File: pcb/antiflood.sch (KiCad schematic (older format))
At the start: 92 parts, among them J1 Barrel_Jack, J10 Screw_Terminal_01x02, J11 Screw_Terminal_01x02, J12 Screw_Terminal_01x02, J13 Screw_Terminal_01x02, J2 01x03, J3 01x03, J4 Conn_02x05_Odd_Even, J5 Conn_02x04_Odd_Even, J6 Conn_02x05_Odd_Even, J7 Conn_02x03_Odd_Even, J8 Screw_Terminal_01x02, J9 Screw_Terminal_01x02, K1 P-5, K2 P-5, Q1 2N3904, Q2 2N3904, SW1 SW_Push, SW2 SW_Push, SW3 SW_Push, U1 LM1117-3.3, U2 ATMEGA328P-AU, U3 LM7805_TO220, U4 MC34063, U6 TP4056, Y1 16MHz

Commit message: Update.
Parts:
- added R? (x2): 10k, symbol R
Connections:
- wire segments 324 -> 326
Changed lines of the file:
@@
 	3800 3300 3800 2600
 Wire Wire Line
-	3800 2600 4700 2600
+	3800 2600 4800 2600
 Connection ~ 4700 2600
 Wire Wire Line
@@
 	3800 3850 3800 3950
 Wire Wire Line
-	3600 3950 4700 3950
+	3600 3950 4800 3950
 Connection ~ 4700 3950
 Wire Wire Line
@@
 Wire Wire Line
 	3600 2950 3900 2950
+$Comp
+L R R?
+U 1 1 5CB71E28
+P 4950 2600
+F 0 "R?" V 5030 2600 50  0000 C CNN
+F 1 "10k" V 4950 2600 50  0000 C CNN
+F 2 "" V 4880 2600 50  0001 C CNN
+F 3 "" H 4950 2600 50  0001 C CNN
+	1    4950 2600
+	0    -1   -1   0
+$EndComp
+$Comp
+L R R?
+U 1 1 5CB72139
+P 4950 3950
+F 0 "R?" V 5030 3950 50  0000 C CNN
+F 1 "10k" V 4950 3950 50  0000 C CNN
+F 2 "" V 4880 3950 50  0001 C CNN
+F 3 "" H 4950 3950 50  0001 C CNN
+	1    4950 3950
+	0    1    1    0
+$EndComp
+Wire Wire Line
+	5100 3950 5350 3950
+Wire Wire Line
+	5100 2600 5350 2600
+Text Label 5150 3950 0    60   ~ 0
+BSTE
+Text Label 5150 2600 0    60   ~ 0
+CHGE
 $EndSCHEMATC

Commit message: Update: remove linear regul
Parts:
- removed U3: LM7805_TO220, TO_SOT_Packages_THT:TO-220-3_Horizontal, symbol LM7805_TO220
- R?: value R -> 10k
- R?: value R -> 12k
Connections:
- wire segments 326 -> 427

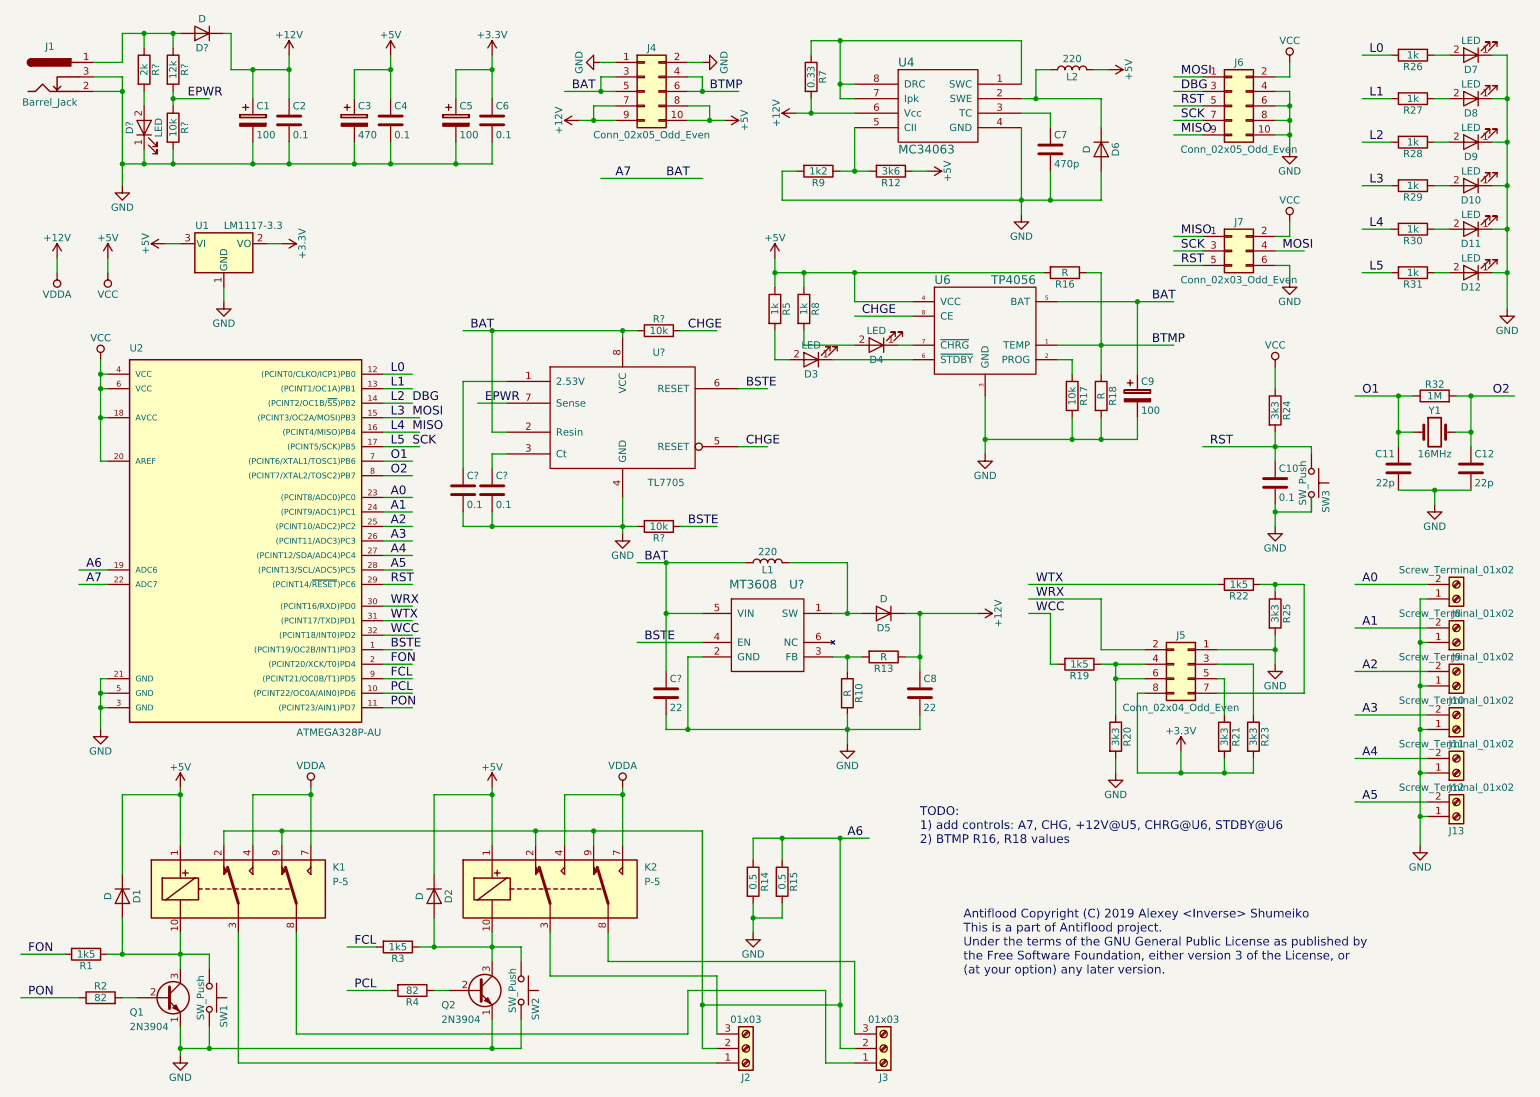
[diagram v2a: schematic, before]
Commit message: Update: pcb-bat connection
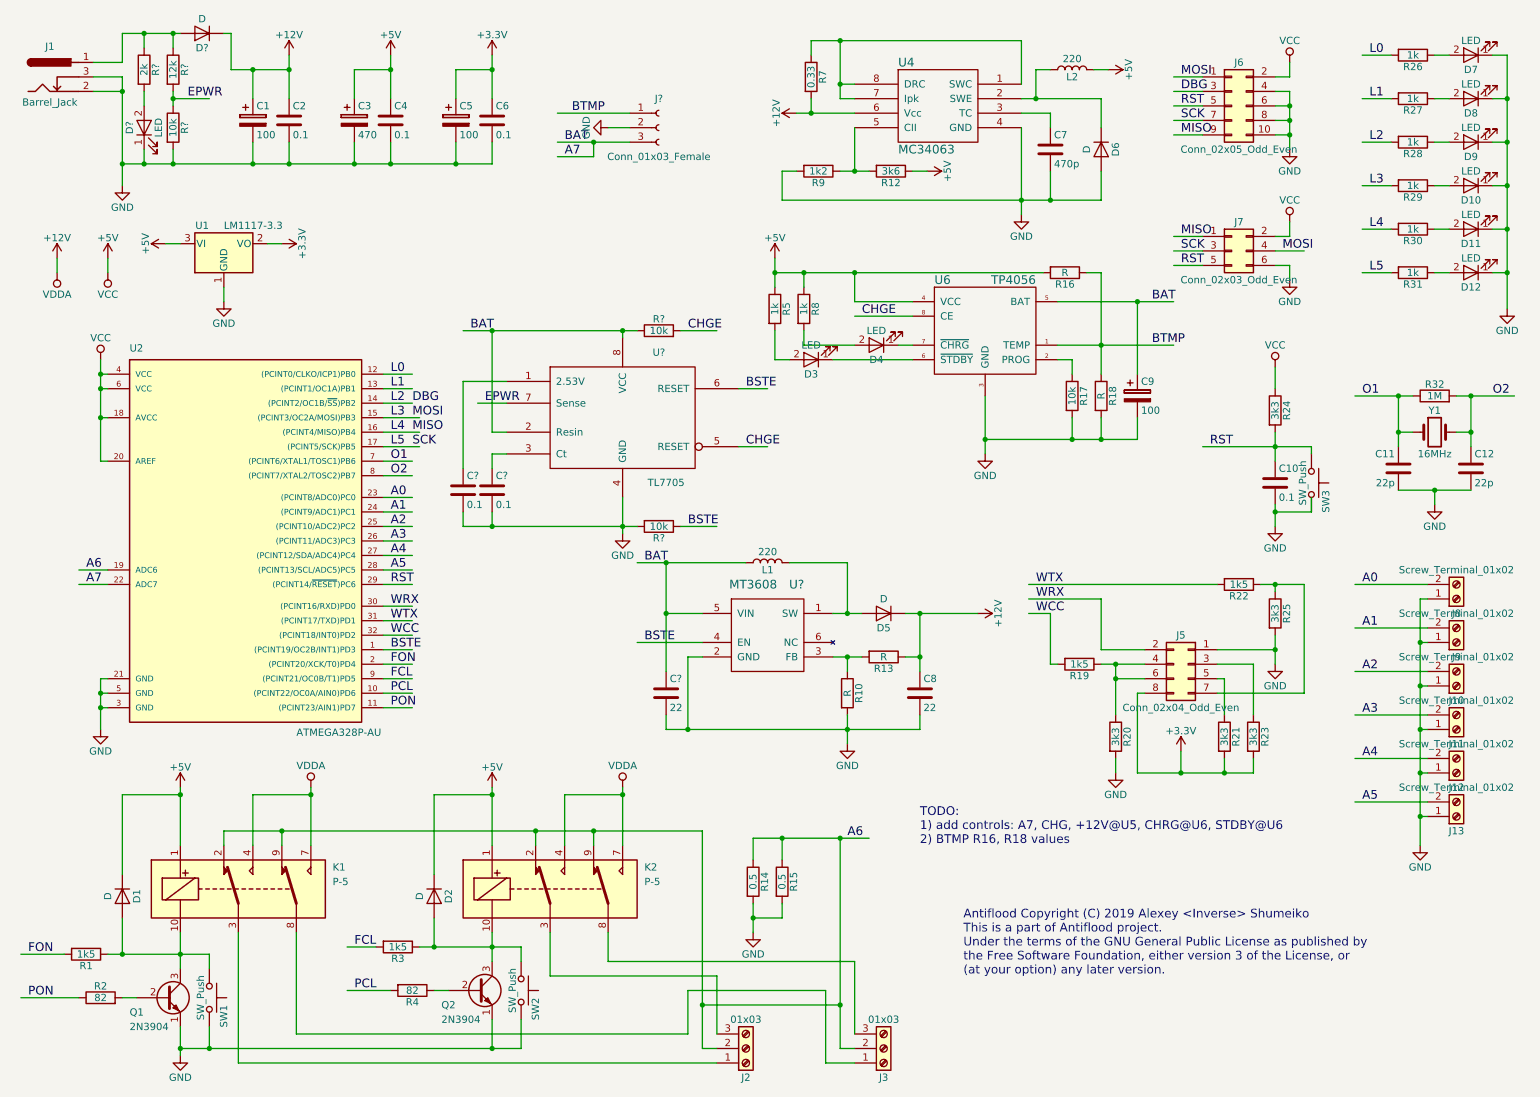
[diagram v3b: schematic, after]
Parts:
- removed J4: Conn_02x05_Odd_Even, Socket_Strips:Socket_Strip_Straight_2x05_Pitch2.54mm, symbol Conn_02x05_Odd_Even
- added J?: Conn_01x03_Female, symbol Conn_01x03_Female
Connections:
- wire segments 427 -> 313

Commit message: Update scheme.
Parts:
- removed D5: D, Diodes_SMD:D_SMA, symbol D
- removed D?: D, symbol D
- removed J?: Conn_01x03_Female, symbol Conn_01x03_Female
- added D?: ???, symbol D_Schottky_x2_KCom_AAK
- added J?: Conn_01x03_Male, symbol Conn_01x03_Male
- added R?: 1k, symbol R
- R10: value R -> 1k05
- R13: value R -> 20k
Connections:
- net labels added: EVSS
- wire segments 313 -> 315
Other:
- note removed: "TODO:\n1) add controls: A7, CHG, +12V@U5, CHRG@U6, STDBY@U6\n2) BTMP R16, R18 values"
- moved on the sheet: U1
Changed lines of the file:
@@
 L +12V #PWR06
 U 1 1 5B464A99
-P 800 2100
-F 0 "#PWR06" H 800 1950 50  0001 C CNN
-F 1 "+12V" H 800 2240 50  0000 C CNN
-F 2 "" H 800 2100 50  0001 C CNN
-F 3 "" H 800 2100 50  0001 C CNN
-	1    800  2100
-	1    0    0    -1
+P 4800 2100
+F 0 "#PWR06" H 4800 1950 50  0001 C CNN
+F 1 "+12V" H 4800 2240 50  0000 C CNN
+F 2 "" H 4800 2100 50  0001 C CNN
+F 3 "" H 4800 2100 50  0001 C CNN
+	1    4800 2100
+	0    -1   -1   0
 $EndComp
 $Comp
 L VDDA #PWR07
 U 1 1 5B464B17
-P 800 2200
-F 0 "#PWR07" H 800 2050 50  0001 C CNN
-F 1 "VDDA" H 800 2350 50  0000 C CNN
-F 2 "" H 800 2200 50  0001 C CNN
-F 3 "" H 800 2200 50  0001 C CNN
-	1    800  2200
-	-1   0    0    1
+P 4900 2100
+F 0 "#PWR07" H 4900 1950 50  0001 C CNN
+F 1 "VDDA" H 4900 2250 50  0000 C CNN
+F 2 "" H 4900 2100 50  0001 C CNN
+F 3 "" H 4900 2100 50  0001 C CNN
+	1    4900 2100
+	0    1    1    0
 $EndComp
 $Comp
@@
 L LM1117-3.3 U1
 U 1 1 5B469F43
-P 1950 2000
-F 0 "U1" H 1800 2125 50  0000 C CNN
-F 1 "LM1117-3.3" H 1950 2125 50  0000 L CNN
-F 2 "TO_SOT_Packages_SMD:SOT-223-3_TabPin2" H 1950 2000 50  0001 C CNN
-F 3 "" H 1950 2000 50  0001 C CNN
-	1    1950 2000
+P 4850 850
+F 0 "U1" H 4700 975 50  0000 C CNN
+F 1 "LM1117-3.3" H 4850 975 50  0000 L CNN
+F 2 "TO_SOT_Packages_SMD:SOT-223-3_TabPin2" H 4850 850 50  0001 C CNN
+F 3 "" H 4850 850 50  0001 C CNN
+	1    4850 850
 	1    0    0    -1
 $EndComp
@@
 L VCC #PWR09
 U 1 1 5B480980
-P 1150 2200
-F 0 "#PWR09" H 1150 2050 50  0001 C CNN
-F 1 "VCC" H 1150 2350 50  0000 C CNN
-F 2 "" H 1150 2200 50  0001 C CNN
-F 3 "" H 1150 2200 50  0001 C CNN
-	1    1150 2200
-	-1   0    0    1
+P 4900 1750
+F 0 "#PWR09" H 4900 1600 50  0001 C CNN
+F 1 "VCC" H 4900 1900 50  0000 C CNN
+F 2 "" H 4900 1750 50  0001 C CNN
+F 3 "" H 4900 1750 50  0001 C CNN
+	1    4900 1750
+	0    1    1    0
 $EndComp
 $Comp
 L +5V #PWR010
 U 1 1 5B480B0B
-P 1150 2100
-F 0 "#PWR010" H 1150 1950 50  0001 C CNN
-F 1 "+5V" H 1150 2240 50  0000 C CNN
-F 2 "" H 1150 2100 50  0001 C CNN
-F 3 "" H 1150 2100 50  0001 C CNN
-	1    1150 2100
-	1    0    0    -1
+P 4800 1750
+F 0 "#PWR010" H 4800 1600 50  0001 C CNN
+F 1 "+5V" H 4800 1890 50  0000 C CNN
+F 2 "" H 4800 1750 50  0001 C CNN
+F 3 "" H 4800 1750 50  0001 C CNN
+	1    4800 1750
+	0    -1   -1   0
 $EndComp
 $Comp
@@
 	1    0    0    -1
 $EndComp
-Text Notes 6750 6150 0    60   ~ 0
-TODO:\n1) add controls: A7, CHG, +12V@U5, CHRG@U6, STDBY@U6\n2) BTMP R16, R18 values
 $Comp
 L C C6
@@
 L GND #PWR036
 U 1 1 5C9B1BA9
-P 1950 2400
-F 0 "#PWR036" H 1950 2150 50  0001 C CNN
-F 1 "GND" H 1950 2250 50  0000 C CNN
-F 2 "" H 1950 2400 50  0001 C CNN
-F 3 "" H 1950 2400 50  0001 C CNN
-	1    1950 2400
+P 4850 1250
+F 0 "#PWR036" H 4850 1000 50  0001 C CNN
+F 1 "GND" H 4850 1100 50  0000 C CNN
+F 2 "" H 4850 1250 50  0001 C CNN
+F 3 "" H 4850 1250 50  0001 C CNN
+	1    4850 1250
 	1    0    0    -1
 $EndComp
@@
 P 6250 5100
 F 0 "R10" V 6330 5100 50  0000 C CNN
-F 1 "R" V 6250 5100 50  0000 C CNN
+F 1 "1k05" V 6250 5100 50  0000 C CNN
 F 2 "Resistors_SMD:R_0805" V 6180 5100 50  0001 C CNN
 F 3 "" H 6250 5100 50  0001 C CNN
@@
 P 6500 4850
 F 0 "R13" V 6580 4850 50  0000 C CNN
-F 1 "R" V 6500 4850 50  0000 C CNN
+F 1 "20k" V 6500 4850 50  0000 C CNN
 F 2 "Resistors_SMD:R_0805" V 6430 4850 50  0001 C CNN
 F 3 "" H 6500 4850 50  0001 C CNN
@@
 $EndComp
 $Comp
-L D D5
-U 1 1 5CAB0B56
-P 6500 4550
-F 0 "D5" H 6500 4650 50  0000 C CNN
-F 1 "D" H 6500 4450 50  0000 C CNN
-F 2 "Diodes_SMD:D_SMA" H 6500 4550 50  0001 C CNN
-F 3 "" H 6500 4550 50  0001 C CNN
-	1    6500 4550
-	-1   0    0    1
-$EndComp
-$Comp
 L GND #PWR046
 U 1 1 5CAB0B68
@@
 L +12V #PWR048
 U 1 1 5CAB3382
-P 7150 4550
-F 0 "#PWR048" H 7150 4400 50  0001 C CNN
-F 1 "+12V" H 7150 4690 50  0000 C CNN
-F 2 "" H 7150 4550 50  0001 C CNN
-F 3 "" H 7150 4550 50  0001 C CNN
-	1    7150 4550
-	0    1    1    0
+P 6650 4250
+F 0 "#PWR048" H 6650 4100 50  0001 C CNN
+F 1 "+12V" H 6650 4390 50  0000 C CNN
+F 2 "" H 6650 4250 50  0001 C CNN
+F 3 "" H 6650 4250 50  0001 C CNN
+	1    6650 4250
+	1    0    0    -1
 $EndComp
 $Comp
@@
 Text Label 4850 4200 0    60   ~ 0
 BAT
-$Comp
-L D D?
-U 1 1 5CB0165B
-P 1800 550
-F 0 "D?" H 1800 650 50  0000 C CNN
-F 1 "D" H 1800 450 50  0000 C CNN
-F 2 "" H 1800 550 50  0001 C CNN
-F 3 "" H 1800 550 50  0001 C CNN
-	1    1800 550
-	-1   0    0    1
-$EndComp
 $Comp
 L R R?
@@
 	9200 2150 9300 2150
 Wire Wire Line
-	1150 2100 1150 2200
+	4800 1750 4900 1750
 Wire Wire Line
 	3050 3600 3250 3600
@@
 	950  4350 1150 4350
 Wire Wire Line
-	800  2100 800  2200
+	4800 2100 4900 2100
 Connection ~ 1250 950
 Wire Wire Line
@@
 Wire Wire Line
 	2150 1000 2150 800
-Wire Wire Line
-	2000 800  2400 800
 Connection ~ 2400 800
 Wire Wire Line
@@
 Connection ~ 3800 800
 Wire Wire Line
-	1550 2000 1650 2000
-Wire Wire Line
-	2250 2000 2350 2000
-Wire Wire Line
-	1950 2300 1950 2400
+	4450 850  4550 850
+Wire Wire Line
+	5150 850  5250 850
+Wire Wire Line
+	4850 1150 4850 1250
 Wire Wire Line
 	5900 1100 6300 1100
@@
 Connection ~ 6250 4550
 Wire Wire Line
-	6650 4550 7150 4550
-Wire Wire Line
 	6250 4200 5850 4200
 Wire Wire Line
-	6750 4550 6750 4950
-Wire Wire Line
-	6750 4850 6650 4850
-Connection ~ 6750 4550
+	6750 4850 6750 4950
+Wire Wire Line
+	6650 4850 7050 4850
 Connection ~ 6750 4850
 Wire Wire Line
@@
 Wire Wire Line
 	1250 750  1250 550
-Connection ~ 2150 800
 Wire Wire Line
 	1600 550  1600 650
@@
 Connection ~ 1600 1000
 Wire Wire Line
-	1250 550  1650 550
+	1250 550  1850 550
 Wire Wire Line
 	1250 1450 3800 1450
-Wire Wire Line
-	1950 550  2000 550
-Wire Wire Line
-	2000 550  2000 800
 Wire Wire Line
 	1400 650  1400 550
@@
 L +3.3V #PWR032
 U 1 1 5C9B0B9F
-P 2350 2000
-F 0 "#PWR032" H 2350 1850 50  0001 C CNN
-F 1 "+3.3V" H 2350 2140 50  0000 C CNN
-F 2 "" H 2350 2000 50  0001 C CNN
-F 3 "" H 2350 2000 50  0001 C CNN
-	1    2350 2000
+P 5250 850
+F 0 "#PWR032" H 5250 700 50  0001 C CNN
+F 1 "+3.3V" H 5250 990 50  0000 C CNN
+F 2 "" H 5250 850 50  0001 C CNN
+F 3 "" H 5250 850 50  0001 C CNN
+	1    5250 850
 	0    1    1    0
 $EndComp
@@
 L +5V #PWR031
 U 1 1 5C9B09BB
-P 1550 2000
-F 0 "#PWR031" H 1550 1850 50  0001 C CNN
-F 1 "+5V" H 1550 2140 50  0000 C CNN
-F 2 "" H 1550 2000 50  0001 C CNN
-F 3 "" H 1550 2000 50  0001 C CNN
-	1    1550 2000
+P 4450 850
+F 0 "#PWR031" H 4450 700 50  0001 C CNN
+F 1 "+5V" H 4450 990 50  0000 C CNN
+F 2 "" H 4450 850 50  0001 C CNN
+F 3 "" H 4450 850 50  0001 C CNN
+	1    4450 850
 	0    -1   -1   0
 $EndComp
@@
 L GND #PWR?
 U 1 1 5CB7D712
-P 4600 1200
-F 0 "#PWR?" H 4600 950 50  0001 C CNN
-F 1 "GND" H 4600 1050 50  0000 C CNN
-F 2 "" H 4600 1200 50  0001 C CNN
-F 3 "" H 4600 1200 50  0001 C CNN
-	1    4600 1200
-	0    1    1    0
-$EndComp
-Wire Wire Line
-	4750 1200 4600 1200
-Wire Wire Line
-	4250 1300 4750 1300
-Text Label 4300 1300 0    60   ~ 0
+P 2250 2100
+F 0 "#PWR?" H 2250 1850 50  0001 C CNN
+F 1 "GND" H 2250 1950 50  0000 C CNN
+F 2 "" H 2250 2100 50  0001 C CNN
+F 3 "" H 2250 2100 50  0001 C CNN
+	1    2250 2100
+	0    1    1    0
+$EndComp
+Wire Wire Line
+	2400 2100 2250 2100
+Wire Wire Line
+	1900 2200 2400 2200
+Text Label 1950 2200 0    60   ~ 0
 BAT
 Wire Wire Line
-	4250 1100 4750 1100
-Text Label 4350 1100 0    60   ~ 0
+	1900 2000 2400 2000
+Text Label 2000 2000 0    60   ~ 0
 BTMP
 Wire Wire Line
-	4500 1300 4500 1400
-Wire Wire Line
-	4500 1400 4250 1400
-Connection ~ 4500 1300
-Text Label 4300 1400 0    60   ~ 0
+	2150 2200 2150 2300
+Wire Wire Line
+	2150 2300 1900 2300
+Connection ~ 2150 2200
+Text Label 1450 2300 0    60   ~ 0
 A7
 $Comp
-L Conn_01x03_Female J?
-U 1 1 5CB81DBA
-P 4950 1200
-F 0 "J?" H 4950 1400 50  0000 C CNN
-F 1 "Conn_01x03_Female" H 4950 1000 50  0000 C CNN
-F 2 "" H 4950 1200 50  0001 C CNN
-F 3 "" H 4950 1200 50  0001 C CNN
-	1    4950 1200
-	1    0    0    -1
-$EndComp
+L Conn_01x03_Male J?
+U 1 1 5CBE3351
+P 2600 2100
+F 0 "J?" H 2600 2300 50  0000 C CNN
+F 1 "Conn_01x03_Male" H 2600 1900 50  0000 C CNN
+F 2 "" H 2600 2100 50  0001 C CNN
+F 3 "" H 2600 2100 50  0001 C CNN
+	1    2600 2100
+	-1   0    0    -1
+$EndComp
+$Comp
+L R R?
+U 1 1 5CBE3722
+P 1750 2300
+F 0 "R?" V 1830 2300 50  0000 C CNN
+F 1 "1k" V 1750 2300 50  0000 C CNN
+F 2 "" V 1680 2300 50  0001 C CNN
+F 3 "" H 1750 2300 50  0001 C CNN
+	1    1750 2300
+	0    1    1    0
+$EndComp
+Wire Wire Line
+	1600 2300 1400 2300
+$Comp
+L D_Schottky_x2_KCom_AAK D?
+U 1 1 5CBE6F53
+P 6650 4550
+F 0 "D?" H 6700 4450 50  0000 C CNN
+F 1 "???" H 6650 4650 50  0000 C CNN
+F 2 "" H 6650 4550 50  0001 C CNN
+F 3 "" H 6650 4550 50  0001 C CNN
+	1    6650 4550
+	1    0    0    1
+$EndComp
+Wire Wire Line
+	6650 4250 6650 4350
+Wire Wire Line
+	7050 4850 7050 4300
+Wire Wire Line
+	7050 4300 6650 4300
+Connection ~ 6650 4300
+Wire Wire Line
+	6950 4550 7300 4550
+Text Label 7100 4550 0    60   ~ 0
+EVSS
+Wire Wire Line
+	2150 800  2400 800
+Text Label 1700 550  0    60   ~ 0
+EVSS
 $EndSCHEMATC

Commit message: Update: scheme, netlist, pcb
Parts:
- removed D?: ???, symbol D_Schottky_x2_KCom_AAK
- added D? (x2): YJ SS14, symbol D_Schottky
- R16: value R -> 10k
- R18: value R -> 19k
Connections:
- wire segments 315 -> 314
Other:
- note added: "V (TEMP) = 0.45 .. 0.8 of Vcc"
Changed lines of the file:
@@
 P 8000 3050
 F 0 "R18" V 8080 3050 50  0000 C CNN
-F 1 "R" V 8000 3050 50  0000 C CNN
+F 1 "19k" V 8000 3050 50  0000 C CNN
 F 2 "Resistors_SMD:R_0805" V 7930 3050 50  0001 C CNN
 F 3 "" H 8000 3050 50  0001 C CNN
@@
 P 7750 2200
 F 0 "R16" V 7830 2200 50  0000 C CNN
-F 1 "R" V 7750 2200 50  0000 C CNN
+F 1 "10k" V 7750 2200 50  0000 C CNN
 F 2 "Resistors_SMD:R_0805" V 7680 2200 50  0001 C CNN
 F 3 "" H 7750 2200 50  0001 C CNN
@@
 L +12V #PWR048
 U 1 1 5CAB3382
-P 6650 4250
-F 0 "#PWR048" H 6650 4100 50  0001 C CNN
-F 1 "+12V" H 6650 4390 50  0000 C CNN
-F 2 "" H 6650 4250 50  0001 C CNN
-F 3 "" H 6650 4250 50  0001 C CNN
-	1    6650 4250
-	1    0    0    -1
+P 6850 4550
+F 0 "#PWR048" H 6850 4400 50  0001 C CNN
+F 1 "+12V" H 6850 4690 50  0000 C CNN
+F 2 "" H 6850 4550 50  0001 C CNN
+F 3 "" H 6850 4550 50  0001 C CNN
+	1    6850 4550
+	0    1    1    0
 $EndComp
 $Comp
@@
 	6250 4200 5850 4200
 Wire Wire Line
-	6750 4850 6750 4950
-Wire Wire Line
-	6650 4850 7050 4850
+	6750 4450 6750 4950
+Wire Wire Line
+	6650 4850 6750 4850
 Connection ~ 6750 4850
 Wire Wire Line
@@
 L GND #PWR?
 U 1 1 5CB7D712
-P 2250 2100
-F 0 "#PWR?" H 2250 1850 50  0001 C CNN
-F 1 "GND" H 2250 1950 50  0000 C CNN
-F 2 "" H 2250 2100 50  0001 C CNN
-F 3 "" H 2250 2100 50  0001 C CNN
-	1    2250 2100
+P 1800 2000
+F 0 "#PWR?" H 1800 1750 50  0001 C CNN
+F 1 "GND" H 1800 1850 50  0000 C CNN
+F 2 "" H 1800 2000 50  0001 C CNN
+F 3 "" H 1800 2000 50  0001 C CNN
+	1    1800 2000
 	0    1    1    0
 $EndComp
-Wire Wire Line
-	2400 2100 2250 2100
 Wire Wire Line
 	1900 2200 2400 2200
 Text Label 1950 2200 0    60   ~ 0
 BAT
-Wire Wire Line
-	1900 2000 2400 2000
-Text Label 2000 2000 0    60   ~ 0
+Text Label 1950 2100 0    60   ~ 0
 BTMP
 Wire Wire Line
@@
 Wire Wire Line
 	1600 2300 1400 2300
-$Comp
-L D_Schottky_x2_KCom_AAK D?
-U 1 1 5CBE6F53
-P 6650 4550
-F 0 "D?" H 6700 4450 50  0000 C CNN
-F 1 "???" H 6650 4650 50  0000 C CNN
-F 2 "" H 6650 4550 50  0001 C CNN
-F 3 "" H 6650 4550 50  0001 C CNN
-	1    6650 4550
-	1    0    0    1
-$EndComp
-Wire Wire Line
-	6650 4250 6650 4350
-Wire Wire Line
-	7050 4850 7050 4300
-Wire Wire Line
-	7050 4300 6650 4300
-Connection ~ 6650 4300
-Wire Wire Line
-	6950 4550 7300 4550
-Text Label 7100 4550 0    60   ~ 0
+Text Label 6450 4050 0    60   ~ 0
 EVSS
 Wire Wire Line
@@
 Text Label 1700 550  0    60   ~ 0
 EVSS
+Text Notes 7700 2550 0    60   ~ 0
+V (TEMP) = 0.45 .. 0.8 of Vcc
+Wire Wire Line
+	2400 2100 1900 2100
+Wire Wire Line
+	2400 2000 1800 2000
+$Comp
+L D_Schottky D?
+U 1 1 5CBF9D2B
+P 6500 4550
+F 0 "D?" H 6500 4650 50  0000 C CNN
+F 1 "YJ SS14" H 6500 4450 50  0000 C CNN
+F 2 "" H 6500 4550 50  0001 C CNN
+F 3 "" H 6500 4550 50  0001 C CNN
+	1    6500 4550
+	-1   0    0    1
+$EndComp
+Wire Wire Line
+	6650 4550 6850 4550
+Connection ~ 6750 4550
+$Comp
+L D_Schottky D?
+U 1 1 5CBFA7E4
+P 6750 4300
+F 0 "D?" H 6750 4400 50  0000 C CNN
+F 1 "YJ SS14" H 6750 4200 50  0000 C CNN
+F 2 "" H 6750 4300 50  0001 C CNN
+F 3 "" H 6750 4300 50  0001 C CNN
+	1    6750 4300
+	0    -1   -1   0
+$EndComp
+Wire Wire Line
+	6750 4150 6750 4050
+Wire Wire Line
+	6750 4050 6400 4050
 $EndSCHEMATC
